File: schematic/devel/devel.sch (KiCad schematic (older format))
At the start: 47 parts, among them J1 CONN_PWR, J2 CONN_X1, J3 CONN_Y2, J4 CONN_X2, J5 CONN_Y1, U1 LM317_SOT223, U2 LM337_SOT223, U3 REF5010IDGK, U4 OPA4197

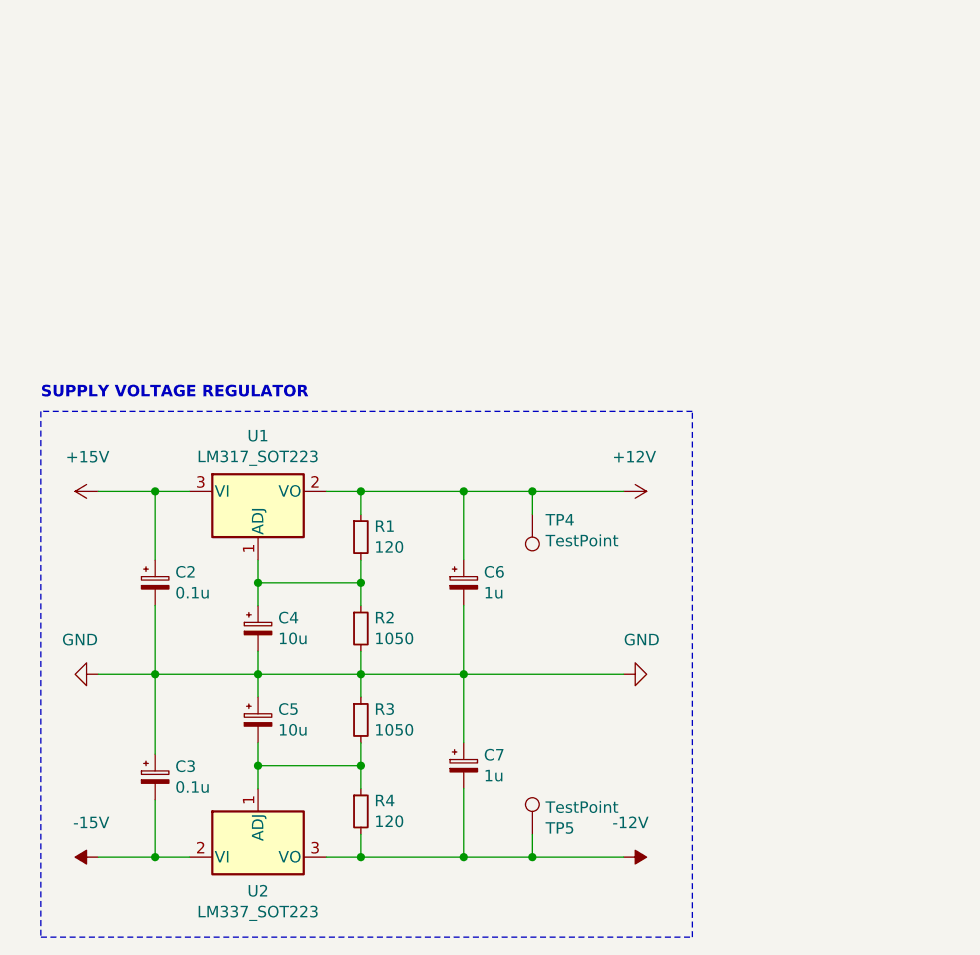
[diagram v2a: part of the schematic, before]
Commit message: added protection diodes to supply voltage regulators
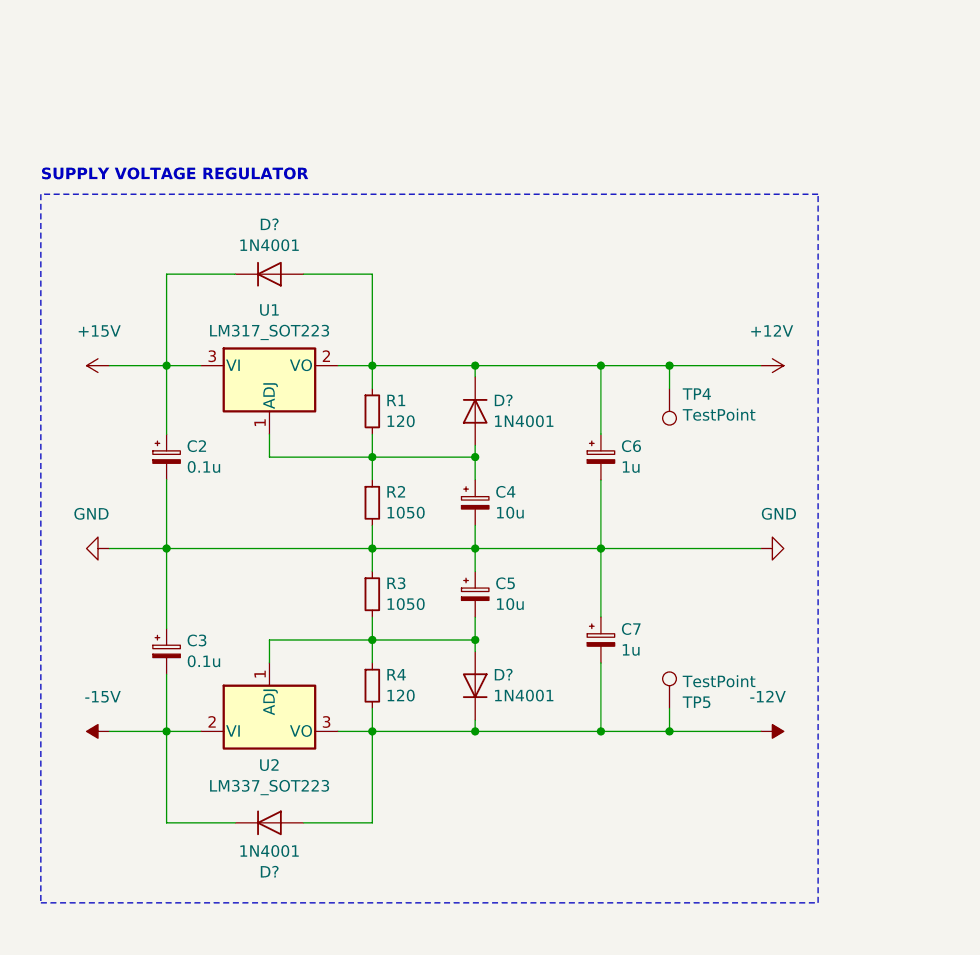
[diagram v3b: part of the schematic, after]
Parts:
- added D? (x4): 1N4001, Diode_THT:D_DO-41_SOD81_P10.16mm_Horizontal, symbol Diode:1N4001
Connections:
- net +12V: now also D?.1 (K), D?.2 (A)
- net +15V: now also D?.1 (K)
- net -12V: now also D?.1 (K), D?.2 (A)
- net -15V: now also D?.1 (K)
- net at C5.2, R3.2, R4.1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: now also D?.2 (A)
- net at C4.1, R1.2, R2.1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: now also D?.2 (A)
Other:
- moved on the sheet: C2, C3, C4, C5, C6, C7, R1, R2, R3, R4, TP4, TP5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

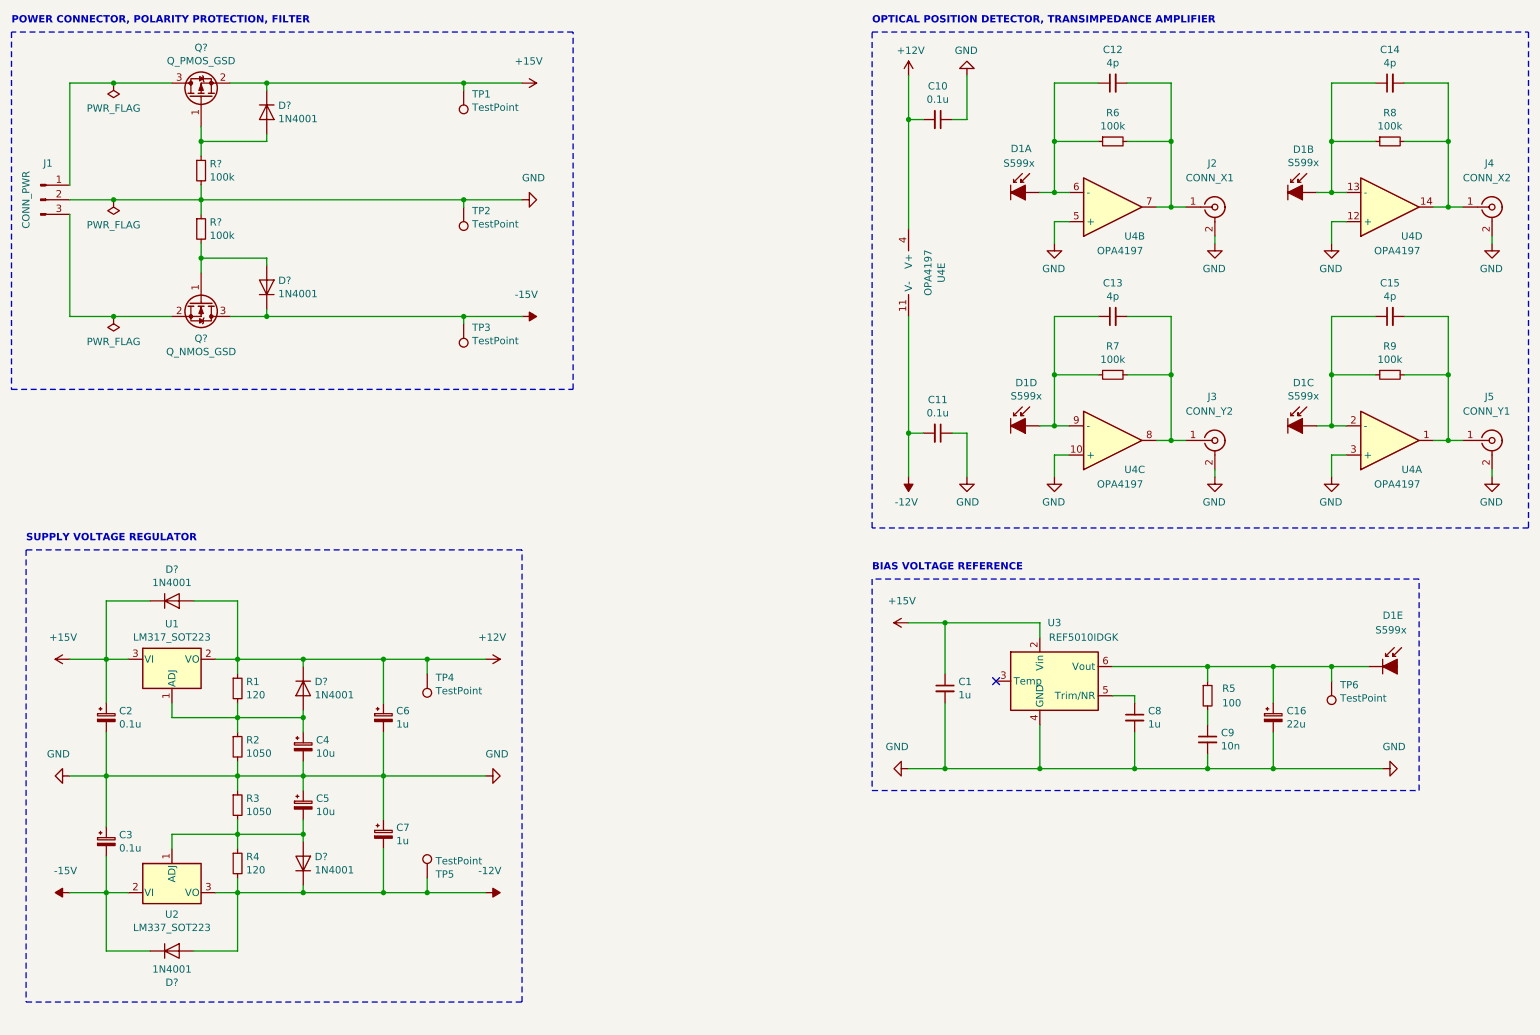
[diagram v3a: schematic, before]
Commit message: fixed details in power connector circuit
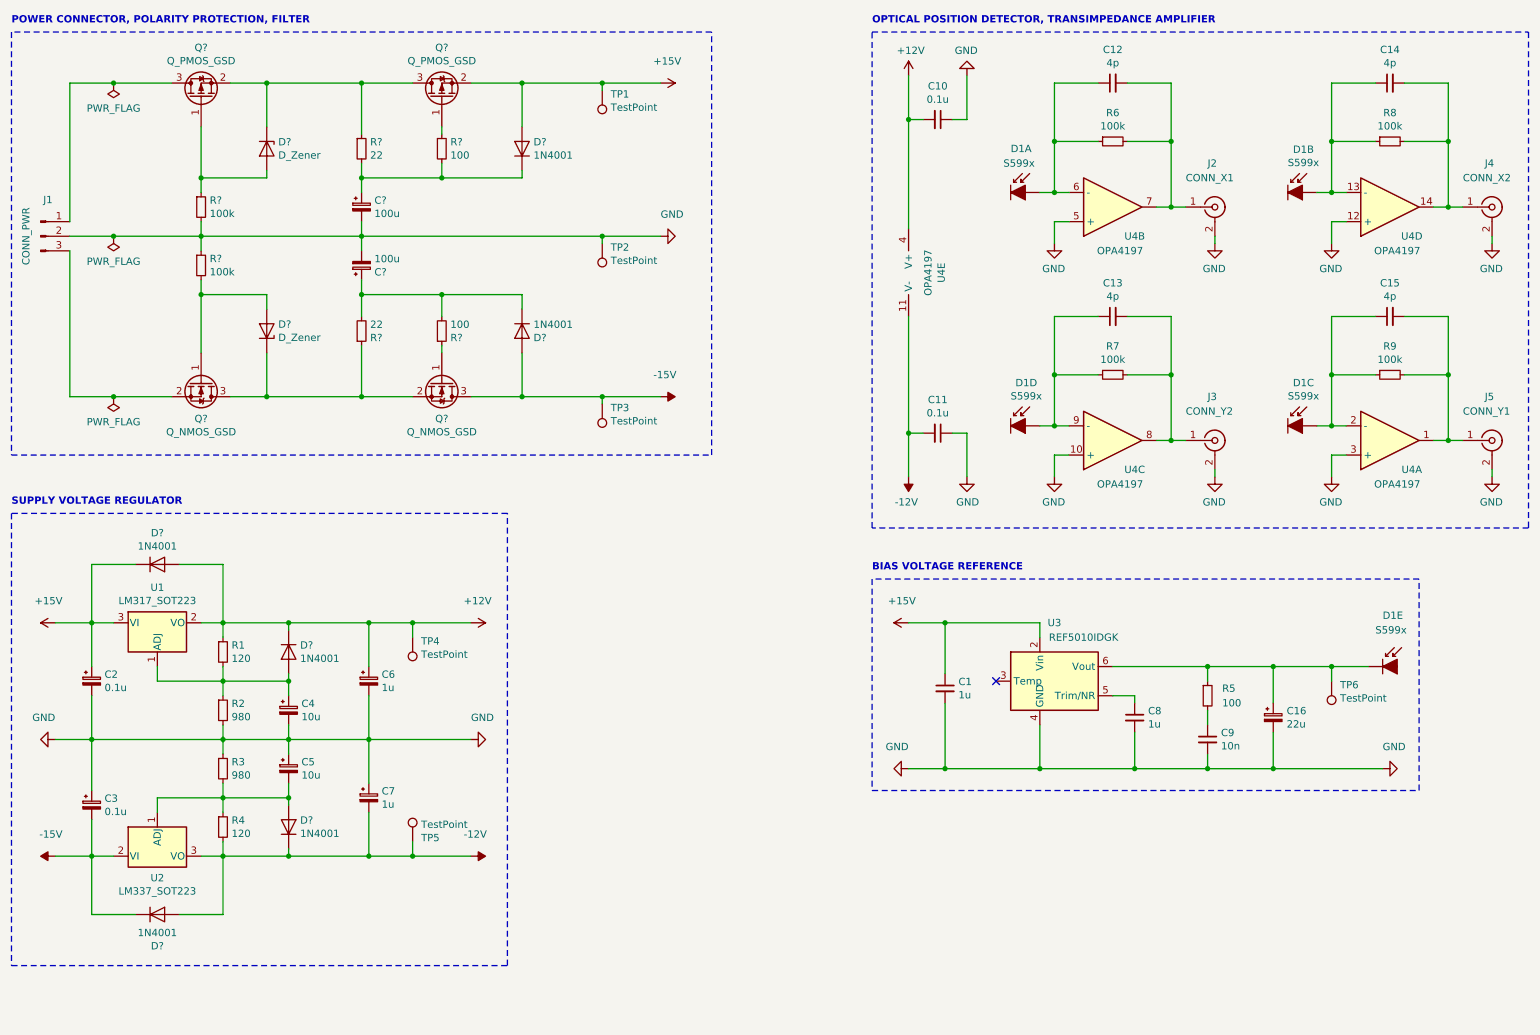
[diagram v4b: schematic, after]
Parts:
- removed D? (x2): 1N4001, Diode_THT:D_DO-41_SOD81_P10.16mm_Horizontal, symbol Diode:1N4001
- added C? (x2): 100u, Capacitor_SMD:CP_Elec_4x3.9, symbol Device:CP_Small
- added D? (x2): 1N4001, Diode_THT:D_DO-41_SOD81_P10.16mm_Horizontal, symbol Diode:1N4001
- added D? (x2): D_Zener, symbol Device:D_Zener
- added Q?: Q_PMOS_GSD, symbol Device:Q_PMOS_GSD
- added Q?: Q_NMOS_GSD, symbol Device:Q_NMOS_GSD
- added R? (x2): 22, symbol Device:R_Small
- added R? (x2): 100, symbol Device:R_Small
- R2, R3: value 1050 -> 980
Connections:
- net +15V: now also D?.2 (A), Q?.2 (S); no longer Q?.2 (S)
- net -15V: now also D?.2 (A), Q?.3 (D); no longer Q?.3 (D)
- net GND: now also C?.2, C?.2
- net at Q?.1 (G), R?.1: now also D?.2 (A)
- net at Q?.1 (G), R?.2: now also D?.2 (A)
- new net: D?.1 (K), Q?.2 (S), Q?.3 (D), R?.1 (x2)
- new net: C?.1, D?.1 (K), R?.2, R?.2 (x2)
- new net: Q?.1 (G), R?.1 (x2)
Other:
- moved on the sheet: C2, C3, C4, C5, C6, C7, D?, J1, Q?, R1, R2, R3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
